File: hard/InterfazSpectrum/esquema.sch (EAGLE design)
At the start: 17 parts, among them IC1 ATMEGA644-20PU, IC2 XC9572-PC44, IC3 LD117AV33, Q3 16 MHz

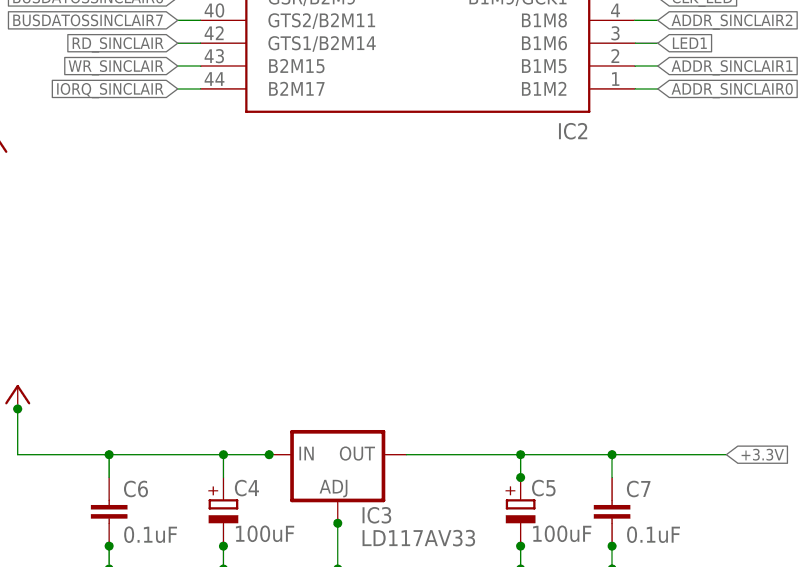
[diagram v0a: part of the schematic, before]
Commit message: Esquema: añadido conector de programacion de cpld. Prueba de posicionado.
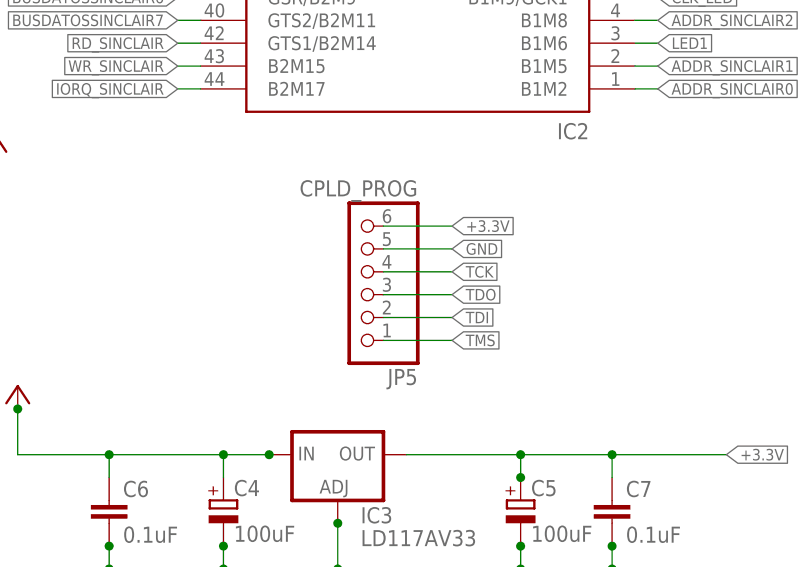
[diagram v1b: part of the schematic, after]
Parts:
- added JP5: CPLD_PROG, pinhead:PINHD-1X6
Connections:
- new net TDO: JP5.3
- net +3.3V: now also JP5.6
- net GND: now also JP5.5
- net TCK: now also JP5.4
- net TDI: now also JP5.2
- net TMS: now also JP5.1
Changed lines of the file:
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@@
 <part name="GND8" library="supply1" deviceset="GND" device=""/>
 <part name="C3" library="rcl" deviceset="C-EU" device="025-025X050" value="0.1uF"/>
+<part name="JP5" library="pinhead" deviceset="PINHD-1X6" device="" value="CPLD_PROG"/>
 </parts>
 <sheets>
@@
 <instance part="GND8" gate="1" x="266.7" y="27.94"/>
 <instance part="C3" gate="G$1" x="101.6" y="121.92"/>
+<instance part="JP5" gate="A" x="238.76" y="63.5" rot="R180"/>
 </instances>
 <busses>
@@
 <junction x="266.7" y="30.48"/>
 <junction x="266.7" y="33.02"/>
+</segment>
+<segment>
+<pinref part="JP5" gate="A" pin="5"/>
+<wire x1="241.3" y1="66.04" x2="248.92" y2="66.04" width="0.1524" layer="91"/>
+<label x="248.92" y="66.04" size="1.27" layer="95" xref="yes"/>
 </segment>
 </net>
@@
 <label x="271.78" y="139.7" size="1.27" layer="95" xref="yes"/>
 </segment>
+<segment>
+<pinref part="JP5" gate="A" pin="3"/>
+<wire x1="241.3" y1="60.96" x2="248.92" y2="60.96" width="0.1524" layer="91"/>
+<label x="248.92" y="60.96" size="1.27" layer="95" xref="yes"/>
+</segment>
 </net>
 <net name="TCK" class="0">
@@
 <label x="271.78" y="137.16" size="1.27" layer="95" xref="yes"/>
 </segment>
+<segment>
+<pinref part="JP5" gate="A" pin="4"/>
+<wire x1="241.3" y1="63.5" x2="248.92" y2="63.5" width="0.1524" layer="91"/>
+<label x="248.92" y="63.5" size="1.27" layer="95" xref="yes"/>
+</segment>
 </net>
 <net name="TMS" class="0">
@@
 <label x="271.78" y="134.62" size="1.27" layer="95" xref="yes"/>
 </segment>
+<segment>
+<pinref part="JP5" gate="A" pin="1"/>
+<wire x1="241.3" y1="55.88" x2="248.92" y2="55.88" width="0.1524" layer="91"/>
+<label x="248.92" y="55.88" size="1.27" layer="95" xref="yes"/>
+</segment>
 </net>
 <net name="TDI" class="0">
@@
 <wire x1="269.24" y1="132.08" x2="271.78" y2="132.08" width="0.1524" layer="91"/>
 <label x="271.78" y="132.08" size="1.27" layer="95" xref="yes"/>
+</segment>
+<segment>
+<pinref part="JP5" gate="A" pin="2"/>
+<wire x1="241.3" y1="58.42" x2="248.92" y2="58.42" width="0.1524" layer="91"/>
+<label x="248.92" y="58.42" size="1.27" layer="95" xref="yes"/>
 </segment>
 </net>
@@
 <label x="218.44" y="139.7" size="1.27" layer="95" rot="R180" xref="yes"/>
 </segment>
-</net>
+<segment>
+<pinref part="JP5" gate="A" pin="6"/>
+<wire x1="241.3" y1="68.58" x2="248.92" y2="68.58" width="0.1524" layer="91"/>
+<label x="248.92" y="68.58" size="1.27" layer="95" xref="yes"/>
+</segment>
+</net>

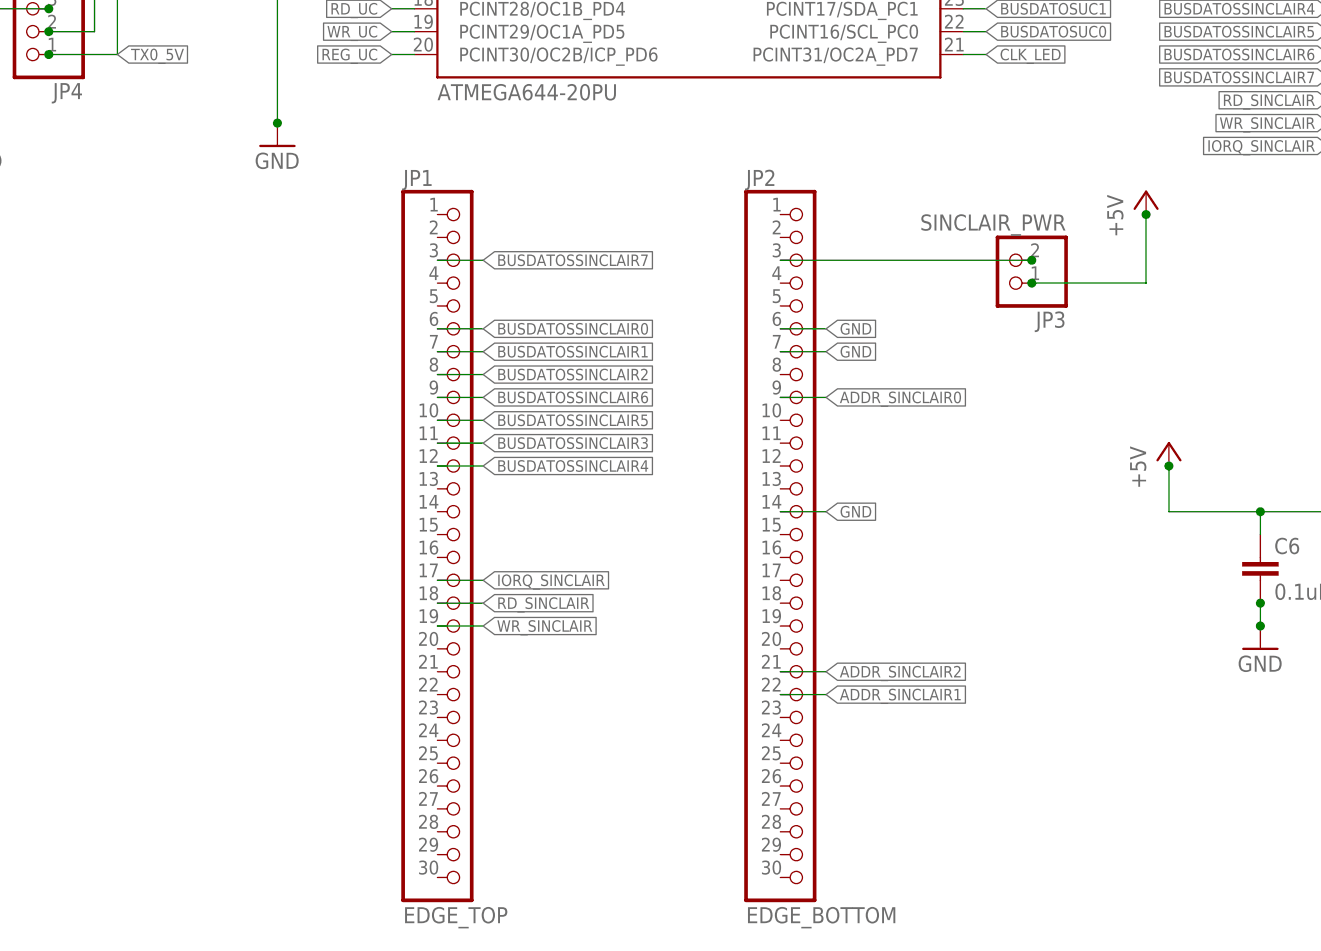
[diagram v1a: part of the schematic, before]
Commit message: Añadido conector Edge y conector del LD1117 vertical
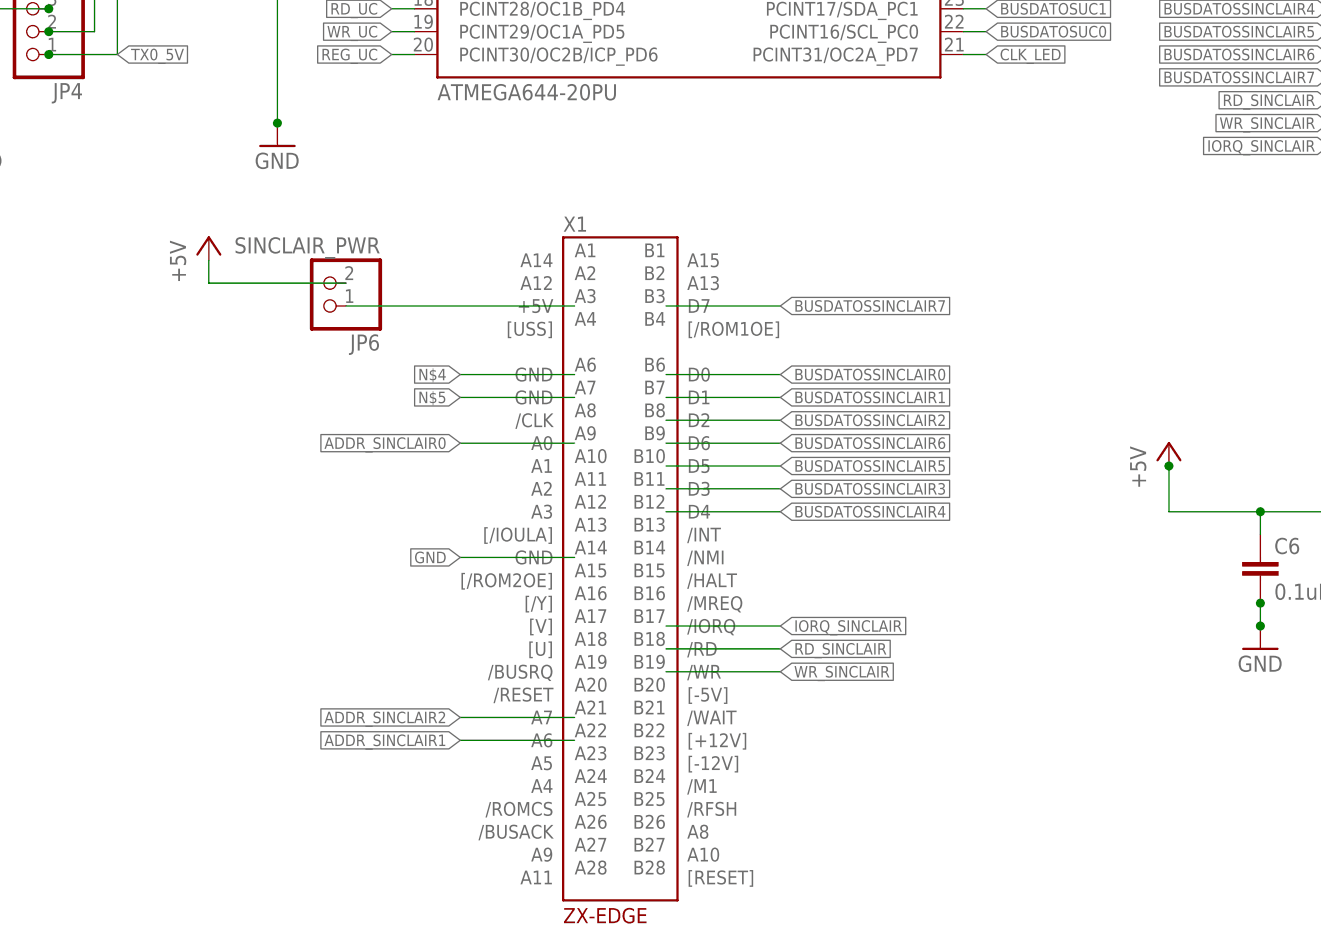
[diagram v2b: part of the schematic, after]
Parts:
- removed JP1: EDGE_TOP, pinhead:PINHD-1X30
- removed JP2: EDGE_BOTTOM, pinhead:PINHD-1X30
- removed JP3: SINCLAIR_PWR, pinhead:PINHD-1X2
- added JP6: SINCLAIR_PWR, pinhead:PINHD-1X2
- added X1: ZX-EDGE, yabus:ZX-EDGE
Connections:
- removed net N$1: JP2.3, JP3.2
- new net N$3: JP6.1, X1.+5V
- new net N$4: X1.GND@1
- new net N$5: X1.GND@2
- net +5V: now also JP6.2; no longer JP3.1
- net ADDR_SINCLAIR0: now also X1.A0; no longer JP2.9
- net ADDR_SINCLAIR1: now also X1.A6; no longer JP2.22
- net ADDR_SINCLAIR2: now also X1.A7; no longer JP2.21
- net BUSDATOSSINCLAIR0: now also X1.D0; no longer JP1.6
- net BUSDATOSSINCLAIR1: now also X1.D1; no longer JP1.7
- net BUSDATOSSINCLAIR2: now also X1.D2; no longer JP1.8
- net BUSDATOSSINCLAIR3: now also X1.D3; no longer JP1.11
- net BUSDATOSSINCLAIR4: now also X1.D4; no longer JP1.12
- net BUSDATOSSINCLAIR5: now also X1.D5; no longer JP1.10
- net BUSDATOSSINCLAIR6: now also X1.D6; no longer JP1.9
- net BUSDATOSSINCLAIR7: now also X1.D7; no longer JP1.3
- net GND: now also X1.GND@3; no longer JP2.14, JP2.6, JP2.7
- net IORQ_SINCLAIR: now also X1./IORQ; no longer JP1.17
- net RD_SINCLAIR: now also X1./RD; no longer JP1.18
- net WR_SINCLAIR: now also X1./WR; no longer JP1.19

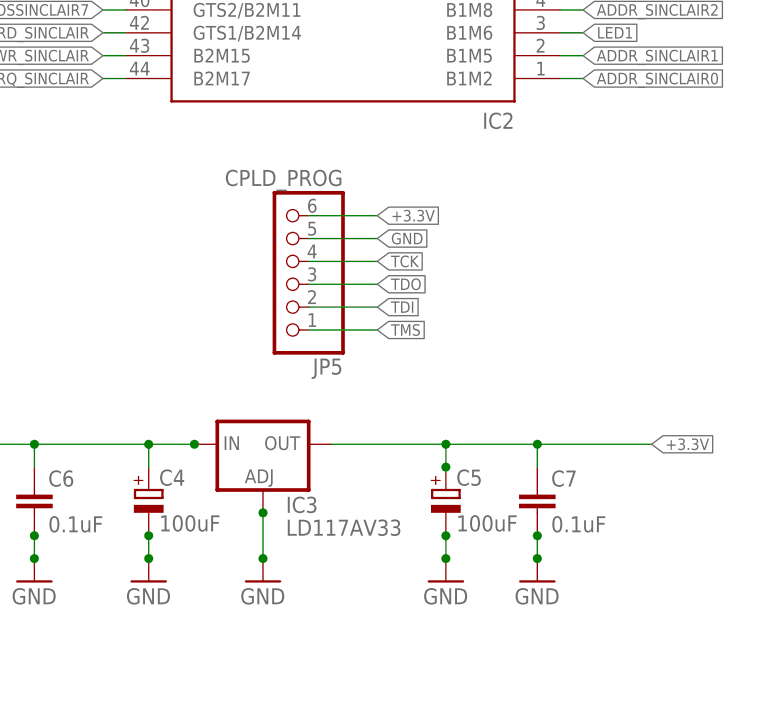
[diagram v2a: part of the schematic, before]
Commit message: Faltaba el fichero de la PCB de eagle
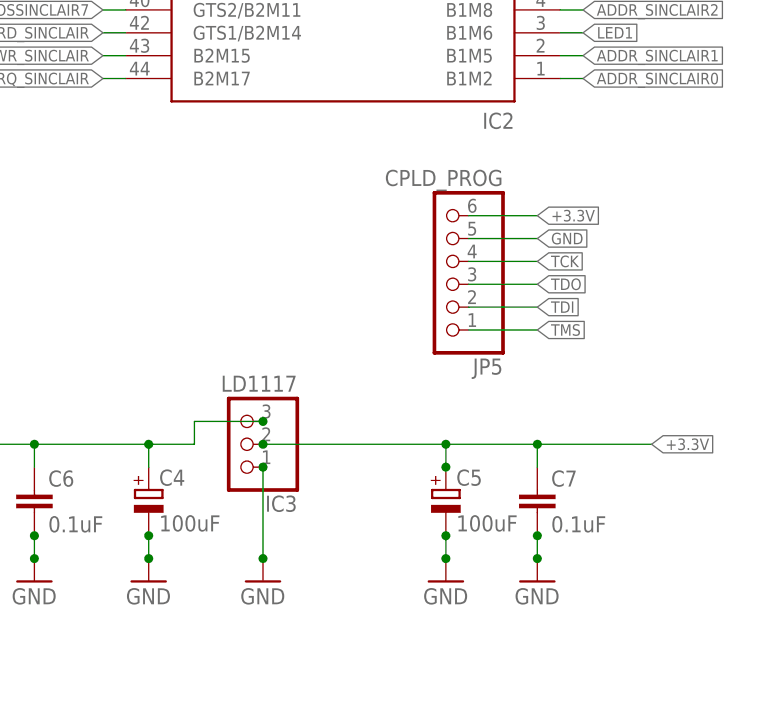
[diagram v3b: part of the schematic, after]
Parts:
- IC3: value LD117AV33 -> LD1117; device v-reg:LD117AV33 -> pinhead:PINHD-1X3
- R1: device resistor:R-EU_0204_2V -> resistor:R-EU_0207_10
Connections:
- net +3.3V: now also IC3.2; no longer IC3.OUT
- net +5V: now also IC3.3; no longer IC3.IN
- net GND: now also IC3.1; no longer IC3.ADJ
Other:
- moved on the sheet: JP5
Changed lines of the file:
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@@
 <part name="C1" library="rcl" deviceset="C-EU" device="025-024X044" value="22 pF"/>
 <part name="C2" library="rcl" deviceset="C-EU" device="025-024X044" value="22pF"/>
-<part name="R1" library="resistor" deviceset="R-EU_" device="0204_2V" value="10K"/>
+<part name="R1" library="resistor" deviceset="R-EU_" device="0207_10" value="10K"/>
 <part name="GND3" library="supply1" deviceset="GND" device=""/>
 <part name="IC1" library="atmel" deviceset="ATMEGA644-*PU" device="" technology="20"/>
@@
 <part name="P+7" library="supply1" deviceset="+5V" device=""/>
 <part name="IC2" library="eOscope" deviceset="XC9572-PC44" device=""/>
-<part name="IC3" library="v-reg" deviceset="LD117A?*" device="V" technology="33"/>
 <part name="GND4" library="supply1" deviceset="GND" device=""/>
 <part name="P+3" library="supply1" deviceset="+5V" device=""/>
@@
 <part name="JP6" library="pinhead" deviceset="PINHD-1X2" device="" value="SINCLAIR_PWR"/>
 <part name="P+5" library="supply1" deviceset="+5V" device=""/>
+<part name="IC3" library="pinhead" deviceset="PINHD-1X3" device="" value="LD1117"/>
 </parts>
 <sheets>
@@
 <instance part="P+7" gate="1" x="66.04" y="111.76"/>
 <instance part="IC2" gate="P" x="248.92" y="106.68" rot="R180"/>
-<instance part="IC3" gate="G$1" x="236.22" y="43.18"/>
 <instance part="GND4" gate="1" x="236.22" y="27.94"/>
 <instance part="P+3" gate="1" x="200.66" y="50.8"/>
@@
 <instance part="GND8" gate="1" x="266.7" y="27.94"/>
 <instance part="C3" gate="G$1" x="101.6" y="121.92"/>
-<instance part="JP5" gate="A" x="238.76" y="63.5" rot="R180"/>
+<instance part="JP5" gate="A" x="256.54" y="63.5" rot="R180"/>
 <instance part="X1" gate="ZX-BUS" x="139.7" y="60.96"/>
 <instance part="JP6" gate="G$1" x="106.68" y="68.58" rot="R180"/>
 <instance part="P+5" gate="1" x="93.98" y="73.66"/>
+<instance part="IC3" gate="A" x="233.68" y="43.18" rot="R180"/>
 </instances>
 <busses>
@@
 </segment>
 <segment>
-<pinref part="IC3" gate="G$1" pin="ADJ"/>
 <pinref part="GND4" gate="1" pin="GND"/>
-<wire x1="236.22" y1="30.48" x2="236.22" y2="35.56" width="0.1524" layer="91"/>
+<wire x1="236.22" y1="30.48" x2="236.22" y2="40.64" width="0.1524" layer="91"/>
 <junction x="236.22" y="30.48"/>
-<junction x="236.22" y="35.56"/>
+<pinref part="IC3" gate="A" pin="1"/>
+<junction x="236.22" y="40.64"/>
 </segment>
 <segment>
@@
 <segment>
 <pinref part="JP5" gate="A" pin="5"/>
-<wire x1="241.3" y1="66.04" x2="248.92" y2="66.04" width="0.1524" layer="91"/>
-<label x="248.92" y="66.04" size="1.27" layer="95" xref="yes"/>
+<wire x1="259.08" y1="66.04" x2="266.7" y2="66.04" width="0.1524" layer="91"/>
+<label x="266.7" y="66.04" size="1.27" layer="95" xref="yes"/>
 </segment>
 <segment>
@@
 <wire x1="200.66" y1="48.26" x2="200.66" y2="43.18" width="0.1524" layer="91"/>
 <junction x="200.66" y="48.26"/>
-<pinref part="IC3" gate="G$1" pin="IN"/>
 <wire x1="200.66" y1="43.18" x2="210.82" y2="43.18" width="0.1524" layer="91"/>
 <pinref part="C4" gate="G$1" pin="+"/>
@@
 <wire x1="223.52" y1="43.18" x2="223.52" y2="40.64" width="0.1524" layer="91"/>
 <junction x="223.52" y="43.18"/>
-<junction x="228.6" y="43.18"/>
 <pinref part="C6" gate="G$1" pin="1"/>
 <wire x1="210.82" y1="40.64" x2="210.82" y2="43.18" width="0.1524" layer="91"/>
 <junction x="210.82" y="43.18"/>
+<pinref part="IC3" gate="A" pin="3"/>
+<wire x1="228.6" y1="43.18" x2="228.6" y2="45.72" width="0.1524" layer="91"/>
+<wire x1="228.6" y1="45.72" x2="236.22" y2="45.72" width="0.1524" layer="91"/>
+<junction x="236.22" y="45.72"/>
 </segment>
 <segment>
@@
 <segment>
 <pinref part="JP5" gate="A" pin="3"/>
-<wire x1="241.3" y1="60.96" x2="248.92" y2="60.96" width="0.1524" layer="91"/>
-<label x="248.92" y="60.96" size="1.27" layer="95" xref="yes"/>
+<wire x1="259.08" y1="60.96" x2="266.7" y2="60.96" width="0.1524" layer="91"/>
+<label x="266.7" y="60.96" size="1.27" layer="95" xref="yes"/>
 </segment>
 </net>
@@
 <segment>
 <pinref part="JP5" gate="A" pin="4"/>
-<wire x1="241.3" y1="63.5" x2="248.92" y2="63.5" width="0.1524" layer="91"/>
-<label x="248.92" y="63.5" size="1.27" layer="95" xref="yes"/>
+<wire x1="259.08" y1="63.5" x2="266.7" y2="63.5" width="0.1524" layer="91"/>
+<label x="266.7" y="63.5" size="1.27" layer="95" xref="yes"/>
 </segment>
 </net>
@@
 <segment>
 <pinref part="JP5" gate="A" pin="1"/>
-<wire x1="241.3" y1="55.88" x2="248.92" y2="55.88" width="0.1524" layer="91"/>
-<label x="248.92" y="55.88" size="1.27" layer="95" xref="yes"/>
+<wire x1="259.08" y1="55.88" x2="266.7" y2="55.88" width="0.1524" layer="91"/>
+<label x="266.7" y="55.88" size="1.27" layer="95" xref="yes"/>
 </segment>
 </net>
@@
 <segment>
 <pinref part="JP5" gate="A" pin="2"/>
-<wire x1="241.3" y1="58.42" x2="248.92" y2="58.42" width="0.1524" layer="91"/>
-<label x="248.92" y="58.42" size="1.27" layer="95" xref="yes"/>
+<wire x1="259.08" y1="58.42" x2="266.7" y2="58.42" width="0.1524" layer="91"/>
+<label x="266.7" y="58.42" size="1.27" layer="95" xref="yes"/>
 </segment>
 </net>
@@
 <wire x1="256.54" y1="40.64" x2="256.54" y2="43.18" width="0.1524" layer="91"/>
 <wire x1="256.54" y1="43.18" x2="266.7" y2="43.18" width="0.1524" layer="91"/>
-<pinref part="IC3" gate="G$1" pin="OUT"/>
 <wire x1="266.7" y1="43.18" x2="279.4" y2="43.18" width="0.1524" layer="91"/>
-<wire x1="243.84" y1="43.18" x2="256.54" y2="43.18" width="0.1524" layer="91"/>
+<wire x1="236.22" y1="43.18" x2="256.54" y2="43.18" width="0.1524" layer="91"/>
 <junction x="256.54" y="40.64"/>
 <junction x="256.54" y="43.18"/>
@@
 <wire x1="266.7" y1="40.64" x2="266.7" y2="43.18" width="0.1524" layer="91"/>
 <junction x="266.7" y="43.18"/>
+<pinref part="IC3" gate="A" pin="2"/>
+<junction x="236.22" y="43.18"/>
 </segment>
 <segment>
@@
 <segment>
 <pinref part="JP5" gate="A" pin="6"/>
-<wire x1="241.3" y1="68.58" x2="248.92" y2="68.58" width="0.1524" layer="91"/>
-<label x="248.92" y="68.58" size="1.27" layer="95" xref="yes"/>
-</segment>
-</net>
+<wire x1="259.08" y1="68.58" x2="266.7" y2="68.58" width="0.1524" layer="91"/>
+<label x="266.7" y="68.58" size="1.27" layer="95" xref="yes"/>
+</segment>
+</net>
